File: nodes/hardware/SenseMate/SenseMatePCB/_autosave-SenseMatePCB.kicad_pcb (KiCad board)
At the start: 2 copper layers, 40.6 x 67.8 mm, 14 parts, among them J1 Conn_01x04, M1 Motor_DC, Q1 2SC1815, Q2 2SC1815, SW5 SW_DPDT_x2

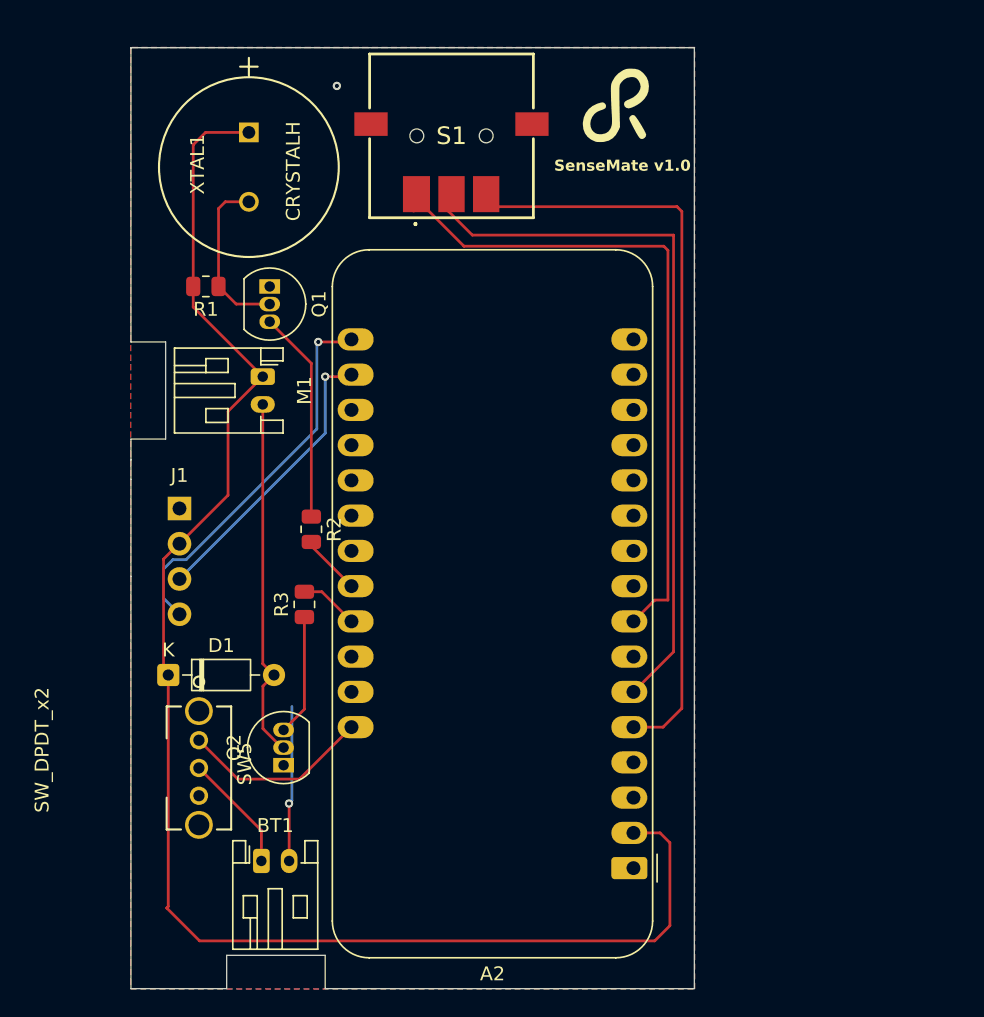
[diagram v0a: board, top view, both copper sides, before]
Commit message: refactored a bit; added pin header on backside for display; moved motor pin jst to side
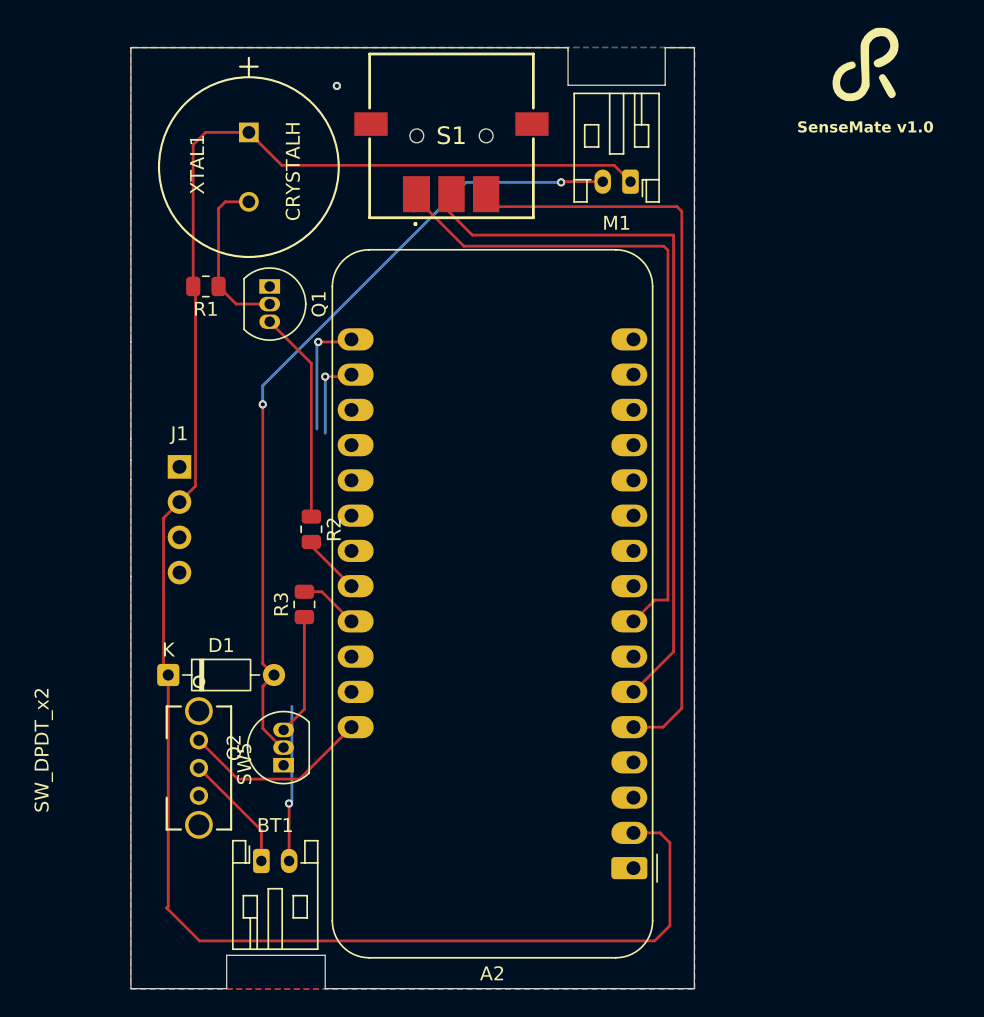
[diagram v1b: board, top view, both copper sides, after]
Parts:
- moved M1 30.0 mm to (115.5, 56.0), turned to 180 degrees
- moved G*** 18.2 mm to (135.0, 47.5)
- moved J1 3.00 mm to (83.0, 76.5)
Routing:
- net Net-(D1-A): track 26.1 -> 58.0 mm, vias 0 -> 2
- net +3V3: track 111.2 -> 136.1 mm
- net Net-(A2-SDA): track 27.7 -> 8.89 mm
- net Net-(A2-SCL): track 21.0 -> 6.03 mm
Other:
- outline, holes or cut-outs redrawn
